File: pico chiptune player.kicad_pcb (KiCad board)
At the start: 4 copper layers, 139.2 x 62.4 mm, 43 parts, among them J2 MicroSD, SW1 Play / Pause, SW2 Next, SW3 Previous, U1 AY-3-8910, U2 0.96"OLED_I2C, U3 PAM8302, U4 YM2149F, U5 PAM8302

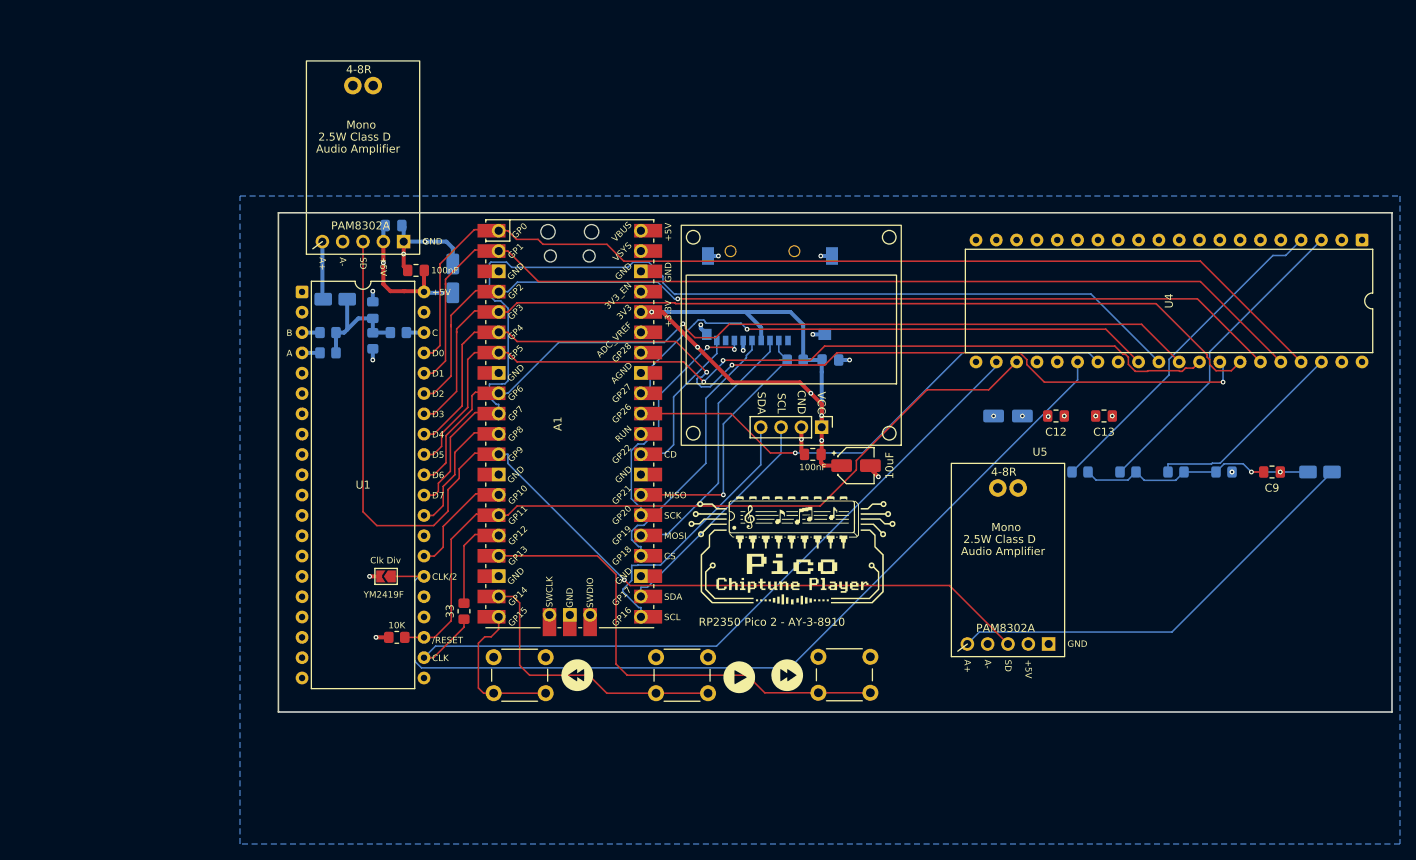
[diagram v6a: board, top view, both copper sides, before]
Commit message: microSD: switch SPI to 4-bit SDIO (Rev 0.6)
Re-map microSD socket J2 from SPI to 4-bit SDIO for the RP2350 PIO
pico_sd_card driver: SD_DAT0..DAT3 -> GPIO18..21, SD_CLK -> GPIO22,
SD_CMD -> GPIO28. Drop the dedicated card-detect switch (presence now
detected in software); R1 10k stays on DAT3. Update HARDWARE.md/README.md
pinout, BOM and revision notes. PCB rerouted: 0 unconnected, 0
shorts/clearance, 12 cosmetic DRC items; ERC clean.
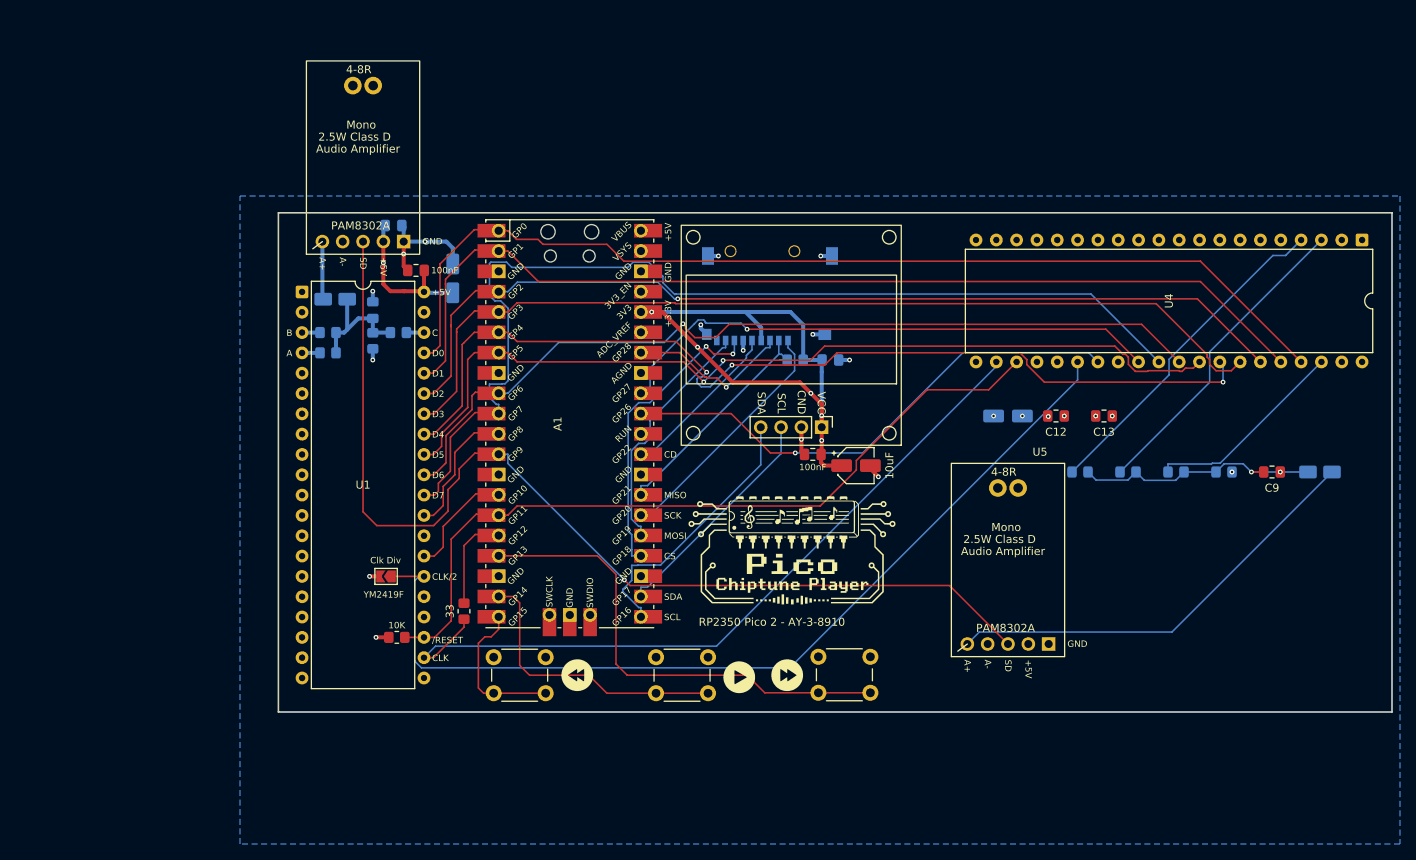
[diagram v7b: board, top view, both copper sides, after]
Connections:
- net /SD_CS renamed /SD_DAT3
- A1 pad 24: /SD_SCK -> /SD_DAT0
- A1 pad 25: /SD_MOSI -> /SD_DAT1
- A1 pad 26: /SD_MISO -> /SD_DAT2
- A1 pad 29: /SD_Card_Detect -> /SD_CLK
- A1 pad 34: unconnected-(A1-GPIO28_ADC2-Pad34) -> /SD_CMD
- J2 pad 1: unconnected-(J2-DAT2-Pad1) -> /SD_DAT2
- J2 pad 3: /SD_MOSI -> /SD_CMD
- J2 pad 5: /SD_SCK -> /SD_CLK
- J2 pad 7: /SD_MISO -> /SD_DAT0
- J2 pad 8: unconnected-(J2-DAT1-Pad8) -> /SD_DAT1
- J2 pad 9: /SD_Card_Detect -> (no net)
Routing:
- net /SD_DAT0: track 0.00 -> 37.9 mm, vias 0 -> 2
- net /SD_SCK: track 34.3 -> 0.00 mm
- net /SD_MOSI: track 33.5 -> 0.00 mm
- net /SD_DAT1: track 0.00 -> 31.0 mm
- net /SD_DAT2: track 0.00 -> 30.8 mm
- net /SD_MISO: track 30.6 -> 0.00 mm, vias 2 -> 0
- net /SD_CMD: track 0.00 -> 20.9 mm, vias 0 -> 1
- net /SD_CLK: track 0.00 -> 20.7 mm
- net /SD_Card_Detect: track 20.4 -> 0.00 mm
- net /SD_DAT3: track 33.3 -> 28.3 mm, vias 1 -> 0

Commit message: pcb: relocate U4/U5 with mirrored passives, resize board, add mounting holes
Move the right-channel PSG (U4) and amp (U5) parallel on the left beside U1/U3, and mirror R9-R12/C9-C13 to match the U1 channel (position, rotation, copper side).

Extend zones and reroute the affected SD/PSG signal nets (0 unconnected). Resize the outline to 118x92mm with rounded corners and add four 3mm NPTH corner mounting holes (H1-H4). Update Rev 0.6 docs and BOM.
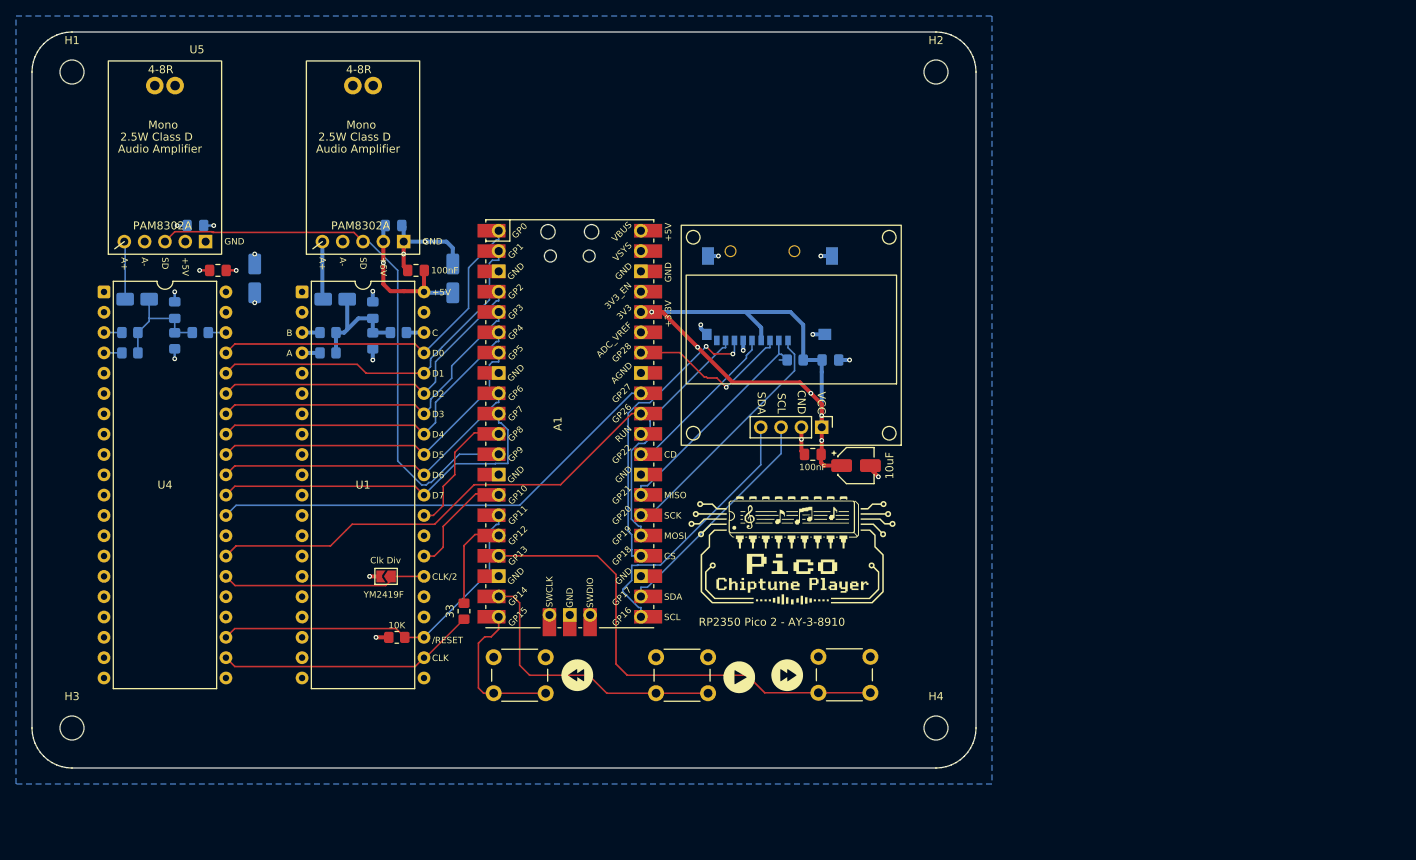
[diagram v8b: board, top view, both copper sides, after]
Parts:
- added H1: MountingHole_3mm, MountingHole_3mm, F.Cu at (83.0, 55.0)
- added H2: MountingHole_3mm, MountingHole_3mm, F.Cu at (191.0, 55.0)
- added H3: MountingHole_3mm, MountingHole_3mm, F.Cu at (83.0, 137.0)
- added H4: MountingHole_3mm, MountingHole_3mm, F.Cu at (191.0, 137.0)
- C13, C9: moved to B.Cu
- moved U4 157.4 mm to (87.0, 82.5), turned to 0 degrees
- moved C10 149.4 mm to (91.1, 83.4), turned to 180 degrees
- moved C9 138.6 mm to (95.8, 84.8), turned to 90 degrees
- moved R12 132.2 mm to (95.8, 88.6), turned to -90 degrees
- moved R10 126.0 mm to (90.2, 87.6)
- moved R11 123.2 mm to (99.0, 87.6), turned to 180 degrees
- moved R9 119.7 mm to (90.2, 90.1)
- moved U5 116.8 mm to (94.6, 65.7)
- moved C13 116.0 mm to (98.4, 74.2)
- moved C12 106.3 mm to (101.2, 79.8), turned to 180 degrees
- moved C11 95.7 mm to (105.8, 80.8), turned to 90 degrees
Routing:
- net /JP1_SEL: track 115.9 -> 25.9 mm
- net /DA7: track 129.6 -> 44.7 mm
- net /DA0: track 128.8 -> 45.0 mm
- net /DA1: track 125.4 -> 45.3 mm
- net /DA4: track 121.5 -> 42.4 mm, vias 3 -> 0
- net /DA2: track 119.2 -> 42.4 mm, vias 1 -> 0
- net /DA3: track 117.1 -> 42.4 mm
- net /DA5: track 112.6 -> 42.7 mm, vias 2 -> 0
- net /DA6: track 108.8 -> 39.9 mm, vias 1 -> 0
- net /CLOCK: track 94.8 -> 32.7 mm
- net /SD_Amp: track 131.7 -> 70.9 mm, vias 1 -> 0
- net /~{RESET}: track 97.6 -> 45.0 mm
- net /AMP2_IN: track 54.5 -> 7.24 mm
- net /ANALOG_A2: track 41.8 -> 2.24 mm
- net /ANALOG_B2: track 39.4 -> 2.24 mm
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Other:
- board size 139.2 x 62.4 mm -> 118 x 92 mm
